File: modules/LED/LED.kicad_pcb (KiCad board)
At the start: 2 copper layers, 40.6 x 40.6 mm, 49 parts, among them J1 2, J10 11, J11 12, J12 13, J13 A0, J14 A1, J15 A2, J16 A3, J17 A4, J18 A5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

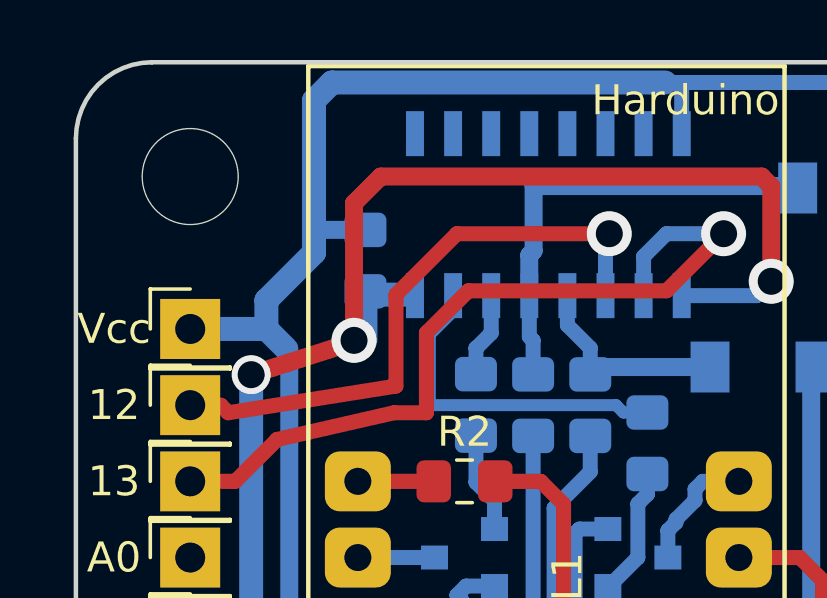
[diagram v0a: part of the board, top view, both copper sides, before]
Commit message: LED small fixes (move cap & silk)
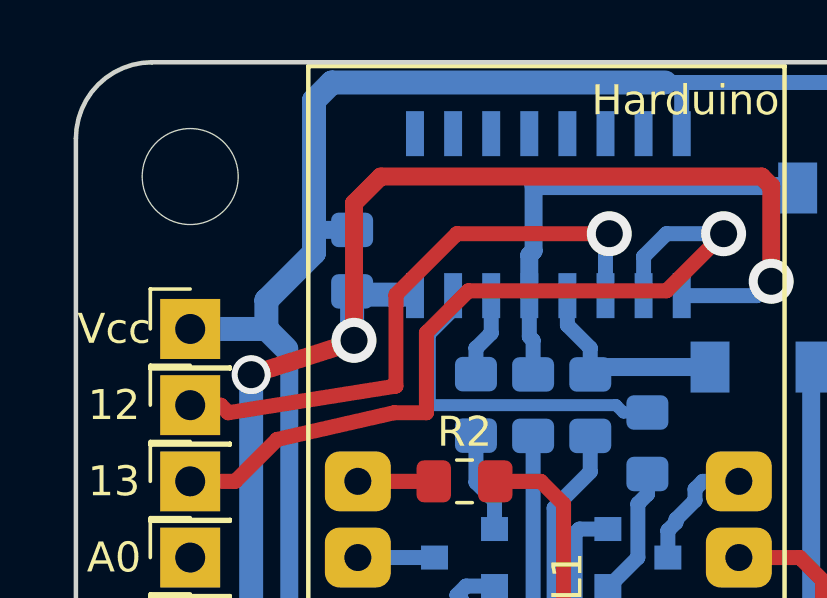
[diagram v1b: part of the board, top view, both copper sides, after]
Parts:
- moved C1 0.44 mm to (98.1, 57.4)
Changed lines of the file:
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@@
     (tags "SOIC 1.27")
     (attr smd)
-    (fp_text reference U2 (at 0 6 90) (layer B.SilkS)
+    (fp_text reference U2 (at 1.5875 6.1595 90) (layer B.SilkS)
       (effects (font (size 1 1) (thickness 0.15)) (justify mirror))
     )
@@
   )
   (module Capacitor_SMD:C_0805_2012Metric_Pad1.15x1.40mm_HandSolder (layer B.Cu)
-    (at 98.552 57.413 270)
+    (at 98.1075 57.413 270)
     (descr "Capacitor SMD 0805 (2012 Metric), square (rectangular) end terminal, IPC_7351 nominal with elongated pad for handsoldering. (Body size source: https://docs.google.com/spreadsheets/d/1BsfQQcO9C6DZCsRaXUlFlo91Tg2WpOkGARC1WS5S8t0/edit?usp=sharing), generated with kicad-footprint-generator")
     (tags "capacitor handsolder")
@@
   (via (at 113.538 79.756) (size 1.5) (drill 0.9) (layers F.Cu B.Cu) (net 45))
   (segment (start 102.489 81.153) (end 102.489 81.153) (width 0.5) (layer F.Cu) (net 45))
-  (via (at 102.489 81.153) (size 1.3) (drill 0.9) (layers F.Cu B.Cu) (net 45) (status 1000000))
+  (via (at 102.489 81.153) (size 1.3) (drill 0.9) (layers F.Cu B.Cu) (net 45))
   (segment (start 102.489 81.153) (end 105.918 81.153) (width 0.5) (layer B.Cu) (net 45))
   (segment (start 107.315 79.756) (end 105.918 81.153) (width 0.5) (layer B.Cu) (net 45))
@@
   (via (at 94.742 61.214) (size 1.3) (drill 0.9) (layers F.Cu B.Cu) (net 48))
   (segment (start 94.9325 82.55) (end 92.71 82.55) (width 0.8) (layer B.Cu) (net 48))
-  (segment (start 98.552 60.071) (end 98.552 58.4835) (width 0.8) (layer B.Cu) (net 48))
-  (segment (start 98.773 58.547) (end 100.076 58.547) (width 0.8) (layer B.Cu) (net 48))
+  (segment (start 98.1075 60.071) (end 98.1075 58.4835) (width 0.8) (layer B.Cu) (net 48))
+  (segment (start 98.7425 58.547) (end 100.0455 58.547) (width 0.8) (layer B.Cu) (net 48))
   (segment (start 97.155 83.82) (end 97.155 88.9) (width 0.8) (layer B.Cu) (net 48))
   (segment (start 97.155 88.9) (end 97.79 89.535) (width 0.8) (layer B.Cu) (net 48))

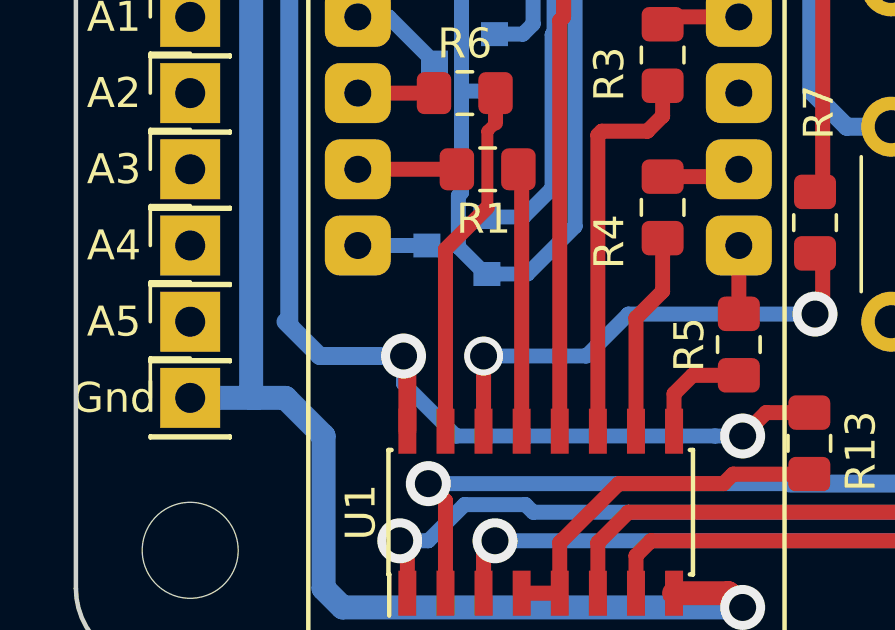
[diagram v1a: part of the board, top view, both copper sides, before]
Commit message: Lost Vcc!!!
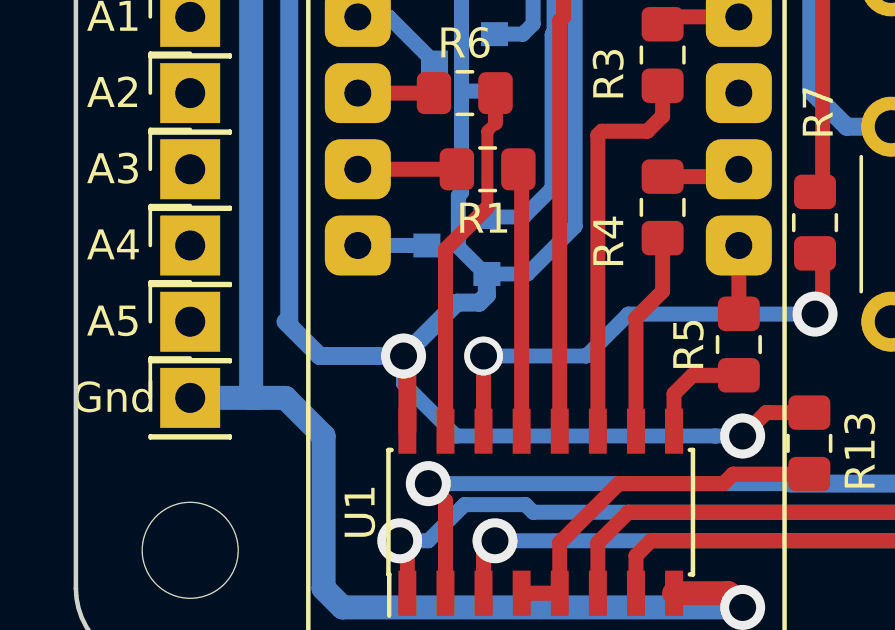
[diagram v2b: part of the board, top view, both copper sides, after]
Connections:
- Q1 pad 2: Net-(Q1-Pad2) -> VCC
- Q2 pad 2: Net-(Q1-Pad2) -> VCC
- Q3 pad 2: Net-(Q1-Pad2) -> VCC
- Q4 pad 2: Net-(Q1-Pad2) -> VCC
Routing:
- net VCC: track 84.2 -> 116.5 mm
- net Net-(Q1-Pad2): track 28.0 -> 0.00 mm

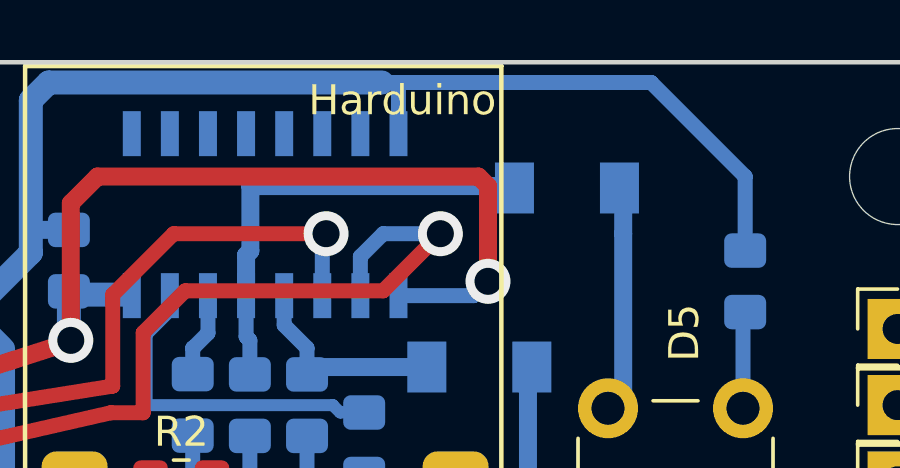
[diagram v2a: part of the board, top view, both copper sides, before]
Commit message: Pull-up 74HS139
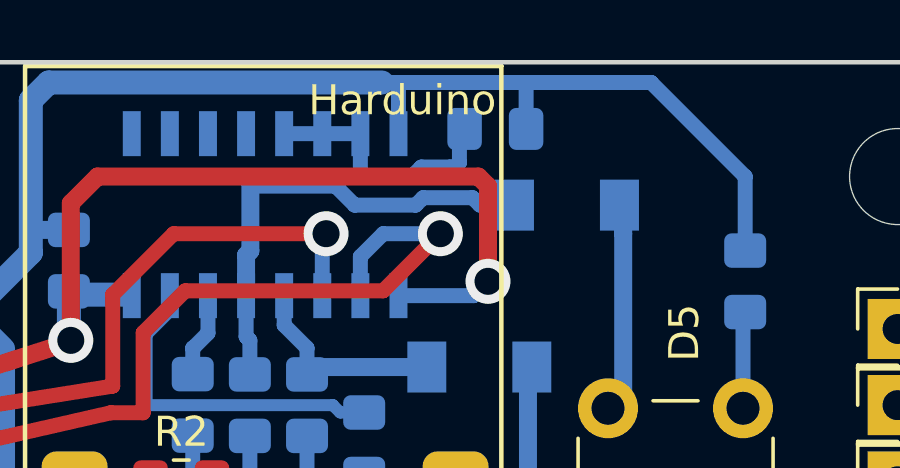
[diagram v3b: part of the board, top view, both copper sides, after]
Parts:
- added R14: R, Resistor_SMD:R_0805_2012Metric_Pad1.15x1.40mm_HandSolder, B.Cu at (112.3, 53.0)
- moved D2 0.57 mm to (114.7, 55.6)
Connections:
- U2 pad 10: (no net) -> Net-(U2-Pad10)
- U2 pad 11: (no net) -> Net-(U2-Pad11)
- U2 pad 12: (no net) -> Net-(U2-Pad12)
- U2 pad 13: (no net) -> Net-(R14-Pad2)
- U2 pad 14: (no net) -> Net-(R14-Pad2)
- U2 pad 15: (no net) -> Net-(R14-Pad2)
- U2 pad 9: (no net) -> Net-(U2-Pad9)
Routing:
- net Net-(R14-Pad2): track 0.00 -> 8.51 mm
- net VCC: track 116.5 -> 118.1 mm
- net Net-(D2-Pad1): track 14.9 -> 15.7 mm

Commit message: LED rework
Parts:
- U1: value 4511 -> 74LS247
- moved R14 36.7 mm to (115.8, 89.5), turned to 270 degrees
- moved C1 11.2 mm to (87.0, 58.5), turned to 90 degrees
- moved U2 2.41 mm to (102.2, 55.9), turned to 270 degrees
- moved Q1 2.22 mm to (107.6, 69.5), turned to 90 degrees
- moved R10 2.01 mm to (104.1, 62.9)
- moved R8 2.01 mm to (108.0, 62.9)
- moved R9 2.01 mm to (102.2, 62.9)
- moved R11 2.01 mm to (106.0, 62.9)
- moved D2 0.33 mm to (114.6, 55.2)
- moved Q3 0.09 mm to (101.9, 71.4)
- moved Q2 0.06 mm to (101.9, 67.3)
- moved U1 0.06 mm to (104.5, 86.4)
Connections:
- J11 pad 1: Net-(J11-Pad1) -> /A0
- J12 pad 1: Net-(J12-Pad1) -> /A1
- R10 pad 1: Net-(Q2-Pad1) -> Net-(Q3-Pad1)
- R11 pad 1: Net-(Q1-Pad1) -> Net-(Q4-Pad1)
- R14 pad 1: VCC -> Net-(R14-Pad1)
- R14 pad 2: Net-(R14-Pad2) -> GND
- R8 pad 1: Net-(Q4-Pad1) -> Net-(Q1-Pad1)
- R9 pad 1: Net-(Q3-Pad1) -> Net-(Q2-Pad1)
- U1 pad 3: Net-(J1-Pad1) -> Net-(R13-Pad1)
- U1 pad 4: Net-(R13-Pad1) -> Net-(U1-Pad4)
- U1 pad 5: Net-(R13-Pad1) -> Net-(R14-Pad1)
- U2 pad 10: Net-(U2-Pad10) -> Net-(R10-Pad2)
- U2 pad 11: Net-(U2-Pad11) -> Net-(D2-Pad1)
- U2 pad 12: Net-(U2-Pad12) -> Net-(D1-Pad1)
- U2 pad 13: Net-(R14-Pad2) -> /A0
- U2 pad 14: Net-(R14-Pad2) -> /A1
- U2 pad 15: Net-(R14-Pad2) -> GND
- U2 pad 2: Net-(J12-Pad1) -> GND
- U2 pad 3: Net-(J11-Pad1) -> GND
- U2 pad 4: Net-(D1-Pad1) -> Net-(U2-Pad4)
- U2 pad 5: Net-(D2-Pad1) -> Net-(U2-Pad5)
- U2 pad 6: Net-(R10-Pad2) -> Net-(U2-Pad6)
- U2 pad 7: Net-(R11-Pad2) -> Net-(U2-Pad7)
- U2 pad 9: Net-(U2-Pad9) -> Net-(R11-Pad2)
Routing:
- net Net-(J12-Pad1): track 26.8 -> 0.00 mm, vias 1 -> 0
- net GND: track 79.7 -> 57.3 mm, vias 4 -> 3
- net Net-(J11-Pad1): track 20.2 -> 0.00 mm, vias 1 -> 0
- net /A1: track 0.00 -> 13.2 mm
- net /A0: track 0.00 -> 13.0 mm
- net Net-(D2-Pad1): track 15.7 -> 4.53 mm
- net Net-(R14-Pad2): track 8.51 -> 0.00 mm
- net Net-(R11-Pad2): track 11.4 -> 3.75 mm
- net Net-(Q3-Pad1): track 8.26 -> 1.43 mm
- net VCC: track 118.1 -> 111.6 mm
- net Net-(D1-Pad1): track 7.11 -> 11.7 mm
- net Net-(Q1-Pad1): track 4.31 -> 0.00 mm
- net Net-(Q4-Pad1): track 15.4 -> 12.5 mm
- net Net-(Q2-Pad1): track 3.37 -> 0.94 mm
- net Net-(L1-Pad7): track 4.22 -> 1.94 mm
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
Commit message: Fix LED pcb
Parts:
- removed R14: R, Resistor_SMD:R_0805_2012Metric_Pad1.15x1.40mm_HandSolder
- moved R12 25.2 mm to (115.8, 82.9), turned to 0 degrees
- moved R13 15.7 mm to (97.8, 86.0)
- moved C1 8.91 mm to (95.9, 59.1)
- moved R8 4.62 mm to (106.7, 67.3)
- moved D2 3.84 mm to (111.3, 57.1)
- moved Q1 1.86 mm to (107.8, 71.4)
- moved D1 0.72 mm to (111.4, 60.3)
- moved Q3 0.06 mm to (101.9, 71.4)
- renumbered L1 to HL1
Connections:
- net Net-(D4-Pad2) renamed /Line0
- net Net-(J3-Pad1) renamed /D0
- net Net-(J4-Pad1) renamed /D1
- net Net-(J5-Pad1) renamed /D2
- net Net-(J6-Pad1) renamed /D3
- U1 pad 5: Net-(R14-Pad1) -> Net-(R13-Pad1)
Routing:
- net Net-(J1-Pad1): track 27.7 -> 0.21 mm, vias 1 -> 0
- net VCC: track 111.6 -> 85.3 mm, vias 2 -> 1
- net GND: track 57.3 -> 77.1 mm
- net /Line0: track 13.7 -> 28.4 mm
- net Net-(D1-Pad1): track 11.7 -> 24.6 mm
- net Net-(D2-Pad2): track 7.24 -> 15.0 mm
- net Net-(D2-Pad1): track 4.53 -> 11.9 mm
- net Net-(D1-Pad2): track 14.5 -> 21.1 mm
- net Net-(HL1-Pad7): track 1.94 -> 8.19 mm
- net Net-(Q3-Pad1): track 1.43 -> 7.62 mm
- net Net-(Q1-Pad1): track 0.00 -> 5.91 mm
- net /A1: track 13.2 -> 17.6 mm, vias 0 -> 2
- net Net-(R13-Pad1): track 10.9 -> 15.2 mm
- net /D2: track 40.7 -> 37.8 mm
- net Net-(Q4-Pad1): track 12.5 -> 14.8 mm
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
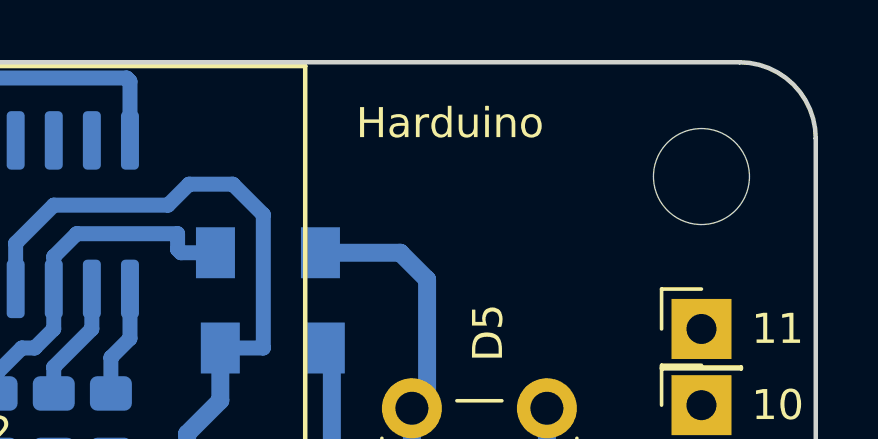
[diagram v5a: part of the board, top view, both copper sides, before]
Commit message: Harduino -> HardDuino
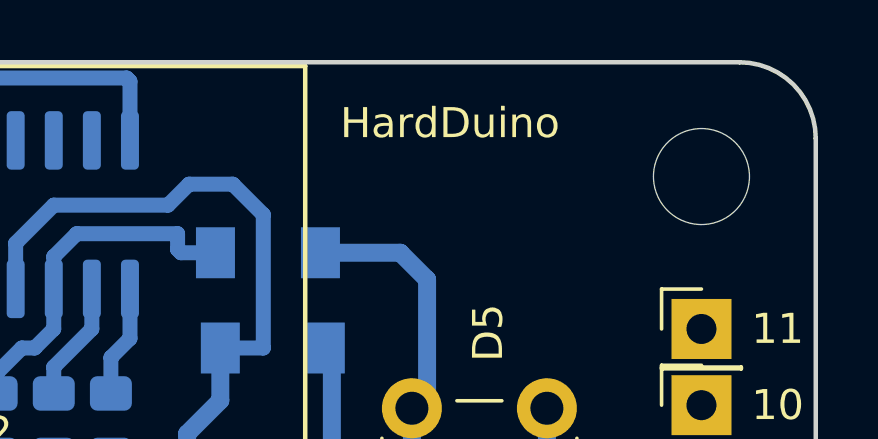
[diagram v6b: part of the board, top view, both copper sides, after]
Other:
- board text added: "HardDuino"
- board text removed: "Harduino"
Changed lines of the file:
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@@
   )
   (setup
-    (last_trace_width 0.5)
+    (last_trace_width 0.3)
     (user_trace_width 0.4)
     (user_trace_width 0.5)
@@
     )
   )
-  (gr_text Harduino (at 117.348 52.832) (layer F.SilkS)
+  (gr_text HardDuino (at 117.348 52.832) (layer F.SilkS)
     (effects (font (size 1 1) (thickness 0.15)))
   )
